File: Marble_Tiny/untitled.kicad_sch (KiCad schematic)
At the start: 72 parts, among them Q3 XTAL_25MHZ_TXC_8Y-25.000MAAJ-T, U12 LP5951MF-3.0/NOPB, U13 LM336M-2.5, U14 DAC8550IDGK, U15 DAC8550IDGK, U16 CDCM61004RHB, U3 Si5351A-B-GT, Y1 OSC_25MHZ_RAKON_IVT3205CR, Y2 VM53S3-25.000-2.5/-30+75, Y3 OSC_20MHZ_IQD_LFVCXO026156

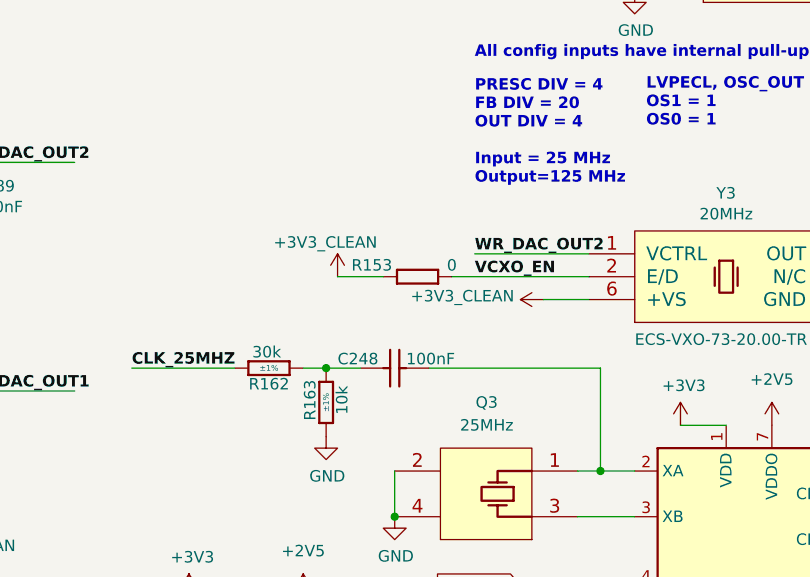
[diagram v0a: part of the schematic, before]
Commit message: connected more address lines to DDR, new board name
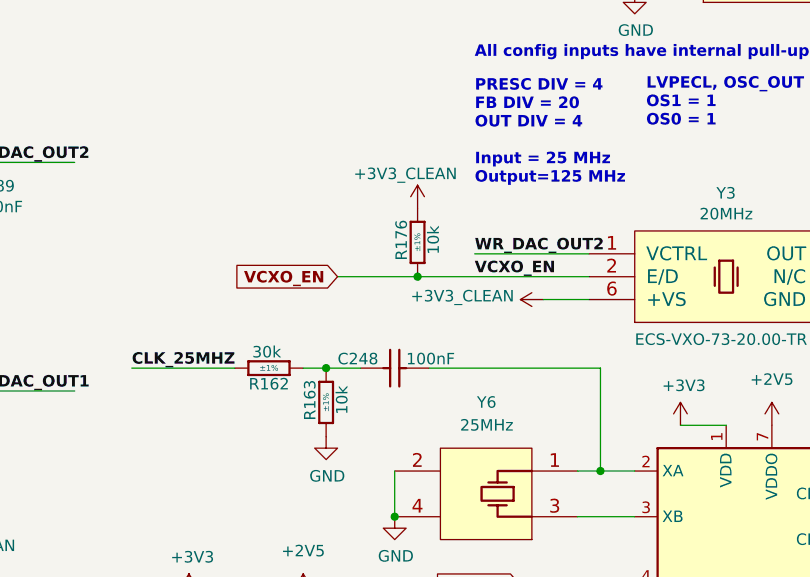
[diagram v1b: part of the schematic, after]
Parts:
- removed R153: R0402_0R_JUMPER, RESC1005X40N, symbol Resistors_SMD:R0402_0R_JUMPER
- added R176: R0402_10K_1%_0.0625W_100PPM, Resistors SMD:RESC1005X40N, symbol Resistors SMD:R0402_10K_1%_0.0625W_100PPM
- renumbered Q3 to Y6
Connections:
- net +3V3_CLEAN: now also R176.2
- net VCXO_EN: now also R176.1
